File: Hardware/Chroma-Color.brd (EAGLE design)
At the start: 106.4 x 50.5 mm, 92 parts, among them J1 15-91-1102, J2 87832-6422, J3 1775470-6, J4 D2514-6V0C-AR-WD, J7 26-64-4040, U1 EP4CE6E22C8N, U2 ADP3338AKCZ-3.3-RL, U3 ADP3338AKCZ-2.5-RL, U4 NCV565ST12T3G, U5 M25P40-VMN6TPBCT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

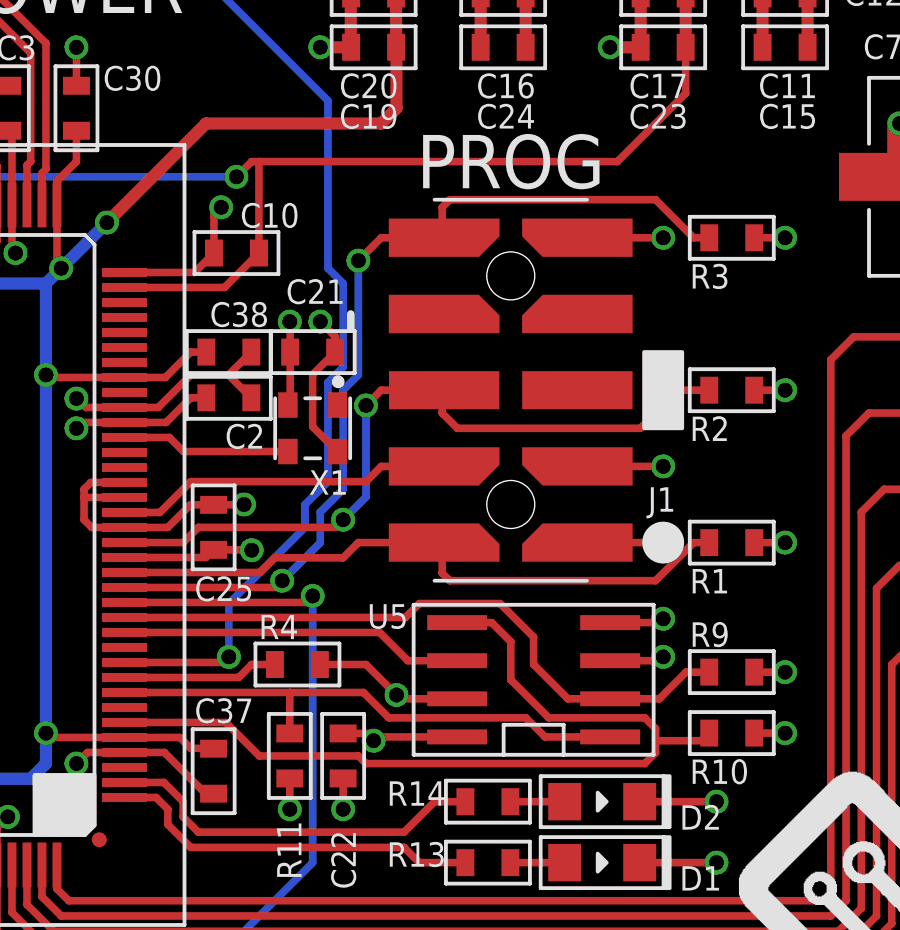
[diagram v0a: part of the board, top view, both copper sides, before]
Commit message: Rev2 start. Fixed JTAG programming cable.
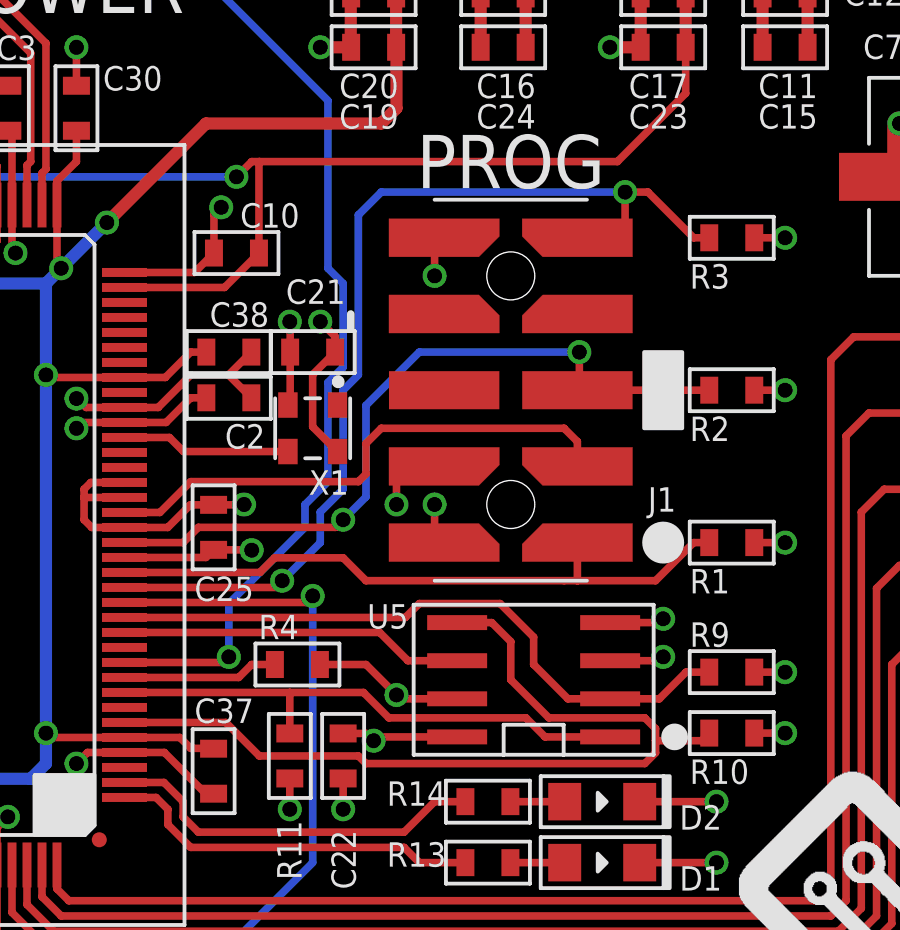
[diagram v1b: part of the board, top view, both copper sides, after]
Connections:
- net 3.3V: now also J1.4; no longer J1.3
- net GND: now also J1.10, J1.2; no longer J1.1, J1.9
- net TCK: now also J1.1; no longer J1.2
- net TDI: now also J1.9; no longer J1.10
- net TDO: now also J1.3; no longer J1.4
- net TMS: now also J1.5; no longer J1.6
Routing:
- net TDO: track 11.3 -> 17.9 mm
- net GND: track 273.3 -> 268.9 mm
- net TDI: track 30.9 -> 34.5 mm

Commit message: Fixed 3 PIN Power Connector.
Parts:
- J7: device PP_Connectors:MOLEX_KK_4_P1 -> PP_Connectors:26-64-4040(KEYPIN1)
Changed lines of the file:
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@@
 <?xml version="1.0" encoding="utf-8"?>
 <!DOCTYPE eagle SYSTEM "eagle.dtd">
-<eagle version="6.5.0">
+<eagle version="6.6.0">
 <drawing>
 <settings>
@@
 <attribute name="NAME" x="89.662" y="8.128" size="1.016" layer="25" font="vector" ratio="16"/>
 </element>
-<element name="J7" library="PP_Connectors" package="MOLEX_KK_4_P1" value="26-64-4040" x="94.996" y="40.386" smashed="yes" rot="R270">
-<attribute name="LABEL02" value="5V" x="100.806" y="37.496" size="1.016" layer="25" font="vector" ratio="16" rot="R90" align="center-left"/>
-<attribute name="LABEL03" value="GND" x="100.702" y="33.178" size="1.016" layer="25" font="vector" ratio="16" rot="R90" align="center-left"/>
-<attribute name="LABEL01" value="12V" x="100.656" y="41.306" size="1.016" layer="25" font="vector" ratio="16" rot="R90" align="center-left"/>
-<attribute name="NAME" x="90.0466" y="31.138" size="1.016" layer="25" font="vector" ratio="16"/>
-</element>
 <element name="C10" library="MF_Passives" package="C0603" value="0.1uF" x="59.944" y="27.178" smashed="yes" rot="R180">
 <attribute name="TOLERANCE" value="N/A" x="59.944" y="27.178" size="1.778" layer="27" rot="R180" display="off"/>
@@
 <element name="FID3" library="MF_Aesthetics" package="FIDUCIAL_0.5MM" value="FIDUCIAL_0.5MM" x="32.766" y="30.226"/>
 <element name="FID4" library="MF_Aesthetics" package="FIDUCIAL_0.5MM" value="FIDUCIAL_0.5MM" x="55.372" y="7.62"/>
+<element name="J7" library="PP_Connectors" package="26-64-4040(KEYPIN1)" value="26-64-4040" x="94.996" y="40.386" smashed="yes" rot="R270">
+<attribute name="LABEL02" value="5V" x="100.806" y="37.75" size="1.016" layer="25" font="vector" ratio="16" rot="R90" align="center-left"/>
+<attribute name="LABEL03" value="GND" x="100.702" y="33.178" size="1.016" layer="25" font="vector" ratio="16" rot="R90" align="center-left"/>
+<attribute name="LABEL01" value="12V" x="100.656" y="41.052" size="1.016" layer="25" font="vector" ratio="16" rot="R90" align="center-left"/>
+<attribute name="NAME" x="101.496" y="48.1294" size="1.016" layer="25" font="vector" ratio="16" rot="R270"/>
+</element>
 </elements>
 <signals>
@@
 <via x="74.168" y="14.986" extent="1-16" drill="0.5"/>
 <wire x1="74.168" y1="14.986" x2="73.152" y2="15.24" width="0.254" layer="2"/>
-<contactref element="J7" pad="4"/>
 <wire x1="8.171" y1="24.071" x2="8.171" y2="22.817" width="0.254" layer="1"/>
 <wire x1="8.171" y1="22.817" x2="8.382" y2="22.606" width="0.254" layer="1"/>
@@
 <wire x1="66.548" y1="17.526" x2="66.548" y2="18.796" width="0.254" layer="1"/>
 <via x="66.548" y="18.796" extent="1-16" drill="0.5"/>
+<contactref element="J7" pad="4"/>
 </signal>
 <signal name="2.5V">
@@
 <contactref element="U3" pad="3"/>
 <contactref element="U4" pad="3"/>
-<contactref element="J7" pad="3"/>
 <wire x1="77.47" y1="41.402" x2="68.58" y2="41.402" width="0.8128" layer="1"/>
 <wire x1="68.58" y1="41.402" x2="68.072" y2="40.894" width="0.8128" layer="1"/>
@@
 <wire x1="86.88" y1="29.972" x2="86.88" y2="29.73" width="0.8128" layer="1"/>
 <wire x1="86.88" y1="29.73" x2="86.868" y2="29.718" width="0.8128" layer="1"/>
-<wire x1="94.996" y1="38.406" x2="97.484" y2="38.406" width="0.8128" layer="1"/>
 <wire x1="97.484" y1="38.406" x2="99.06" y2="36.83" width="0.8128" layer="1"/>
 <wire x1="99.06" y1="36.83" x2="99.06" y2="30.988" width="0.8128" layer="1"/>
@@
 <wire x1="86.301484375" y1="41.402" x2="77.47" y2="41.402" width="0.8128" layer="1"/>
 <contactref element="C9" pad="P$1"/>
-<wire x1="87.134" y1="29.718" x2="87.028" y2="29.718" width="0" layer="19" extent="1-1"/>
+<contactref element="J7" pad="3"/>
+<wire x1="87.028" y1="29.718" x2="87.134" y2="29.718" width="0" layer="19" extent="1-1"/>
+<wire x1="97.484" y1="38.406" x2="94.996" y2="38.406" width="0.8128" layer="1"/>
 </signal>
 <signal name="CLK_50">
@@
 <contactref element="J3" pad="P$5"/>
 <contactref element="J3" pad="P$6"/>
-<contactref element="J7" pad="2"/>
-<wire x1="94.996" y1="42.366" x2="94.996" y2="46.228" width="0.6096" layer="1"/>
 <wire x1="94.996" y1="46.228" x2="91.948" y2="49.276" width="0.6096" layer="1"/>
 <wire x1="91.948" y1="49.276" x2="56.562" y2="49.276" width="0.6096" layer="1"/>
@@
 <wire x1="54.562" y1="48.466" x2="54.562" y2="43.942" width="0.6096" layer="1"/>
 <wire x1="56.562" y1="43.942" x2="56.562" y2="49.276" width="0.6096" layer="1"/>
+<contactref element="J7" pad="2"/>
+<wire x1="94.996" y1="46.228" x2="94.996" y2="42.366" width="0.6096" layer="1"/>
 </signal>
 <signal name="PIN_1">

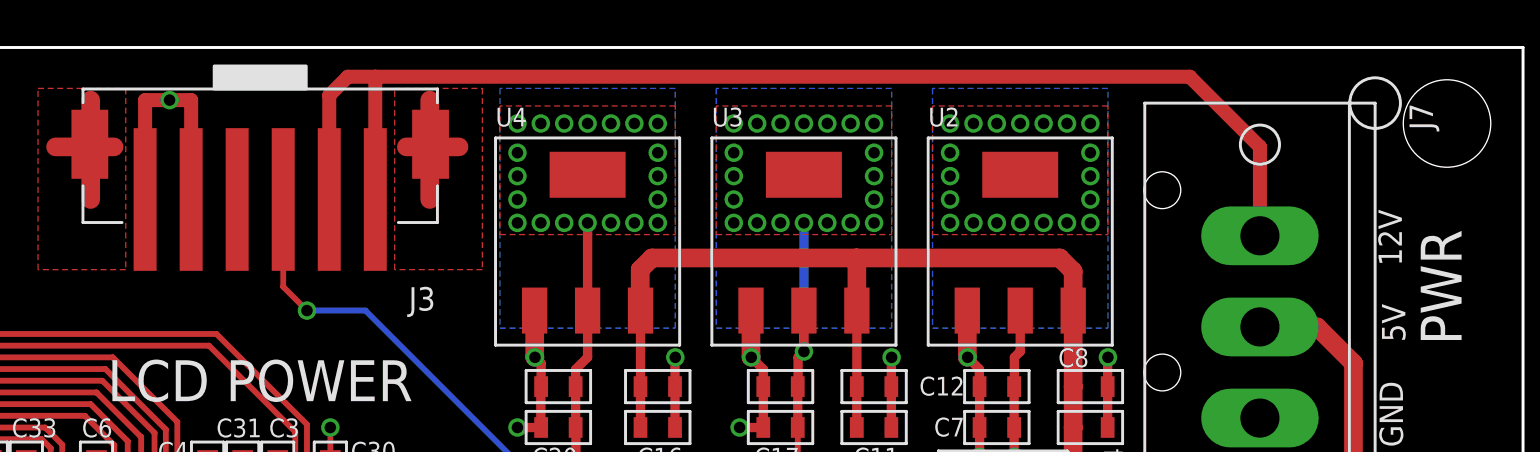
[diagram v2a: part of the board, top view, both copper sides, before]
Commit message: Updated connectors to latest library
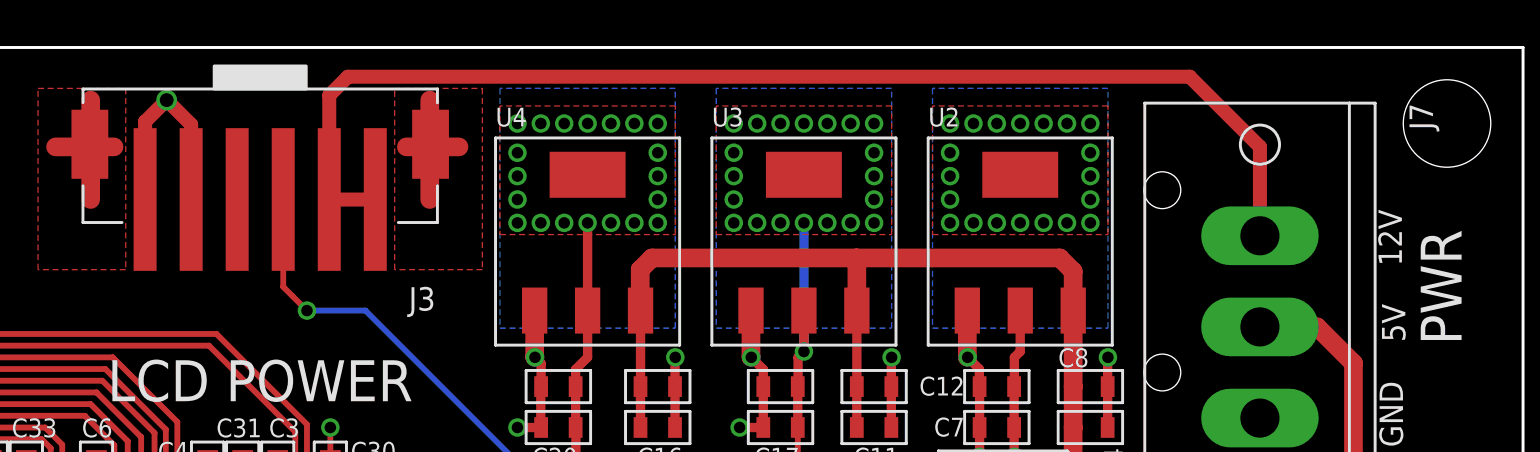
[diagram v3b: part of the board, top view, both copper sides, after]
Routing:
- net 12V: track 55.8 -> 52.4 mm
- net GND: track 268.9 -> 267.8 mm
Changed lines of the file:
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@@
 <attribute name="LABEL28" value="" x="-6.858" y="80.01" size="1.778" layer="27" rot="R180" display="off"/>
 <attribute name="LABEL29" value="" x="-6.858" y="80.01" size="1.778" layer="27" rot="R180" display="off"/>
-<attribute name="LABEL00" value="" x="-6.858" y="80.01" size="1.778" layer="27" rot="R180" display="off"/>
 <attribute name="LABEL01" value="" x="-6.858" y="80.01" size="1.778" layer="27" rot="R180" display="off"/>
 <attribute name="LABEL02" value="" x="-6.858" y="80.01" size="1.778" layer="27" rot="R180" display="off"/>
-</element>
-<element name="J3" library="PP_Connectors" package="1775470-6" value="1775470-6" x="51.562" y="43.942" rot="R180">
-<attribute name="LABEL02" value="" x="5.842" y="104.902" size="1.778" layer="27" rot="R180" display="off"/>
-<attribute name="LABEL03" value="" x="5.842" y="104.902" size="1.778" layer="27" rot="R180" display="off"/>
-<attribute name="LABEL04" value="" x="5.842" y="104.902" size="1.778" layer="27" rot="R180" display="off"/>
-<attribute name="LABEL05" value="" x="5.842" y="104.902" size="1.778" layer="27" rot="R180" display="off"/>
-<attribute name="LABEL00" value="" x="5.842" y="104.902" size="1.778" layer="27" rot="R180" display="off"/>
-<attribute name="LABEL01" value="" x="5.842" y="104.902" size="1.778" layer="27" rot="R180" display="off"/>
+<attribute name="LABEL30" value="" x="22.352" y="44.45" size="1.778" layer="27" rot="R180" display="off"/>
 </element>
 <element name="C22" library="MF_Passives" package="C0603" value="0.1uF" x="63.5" y="10.414" smashed="yes" rot="R270">
@@
 <attribute name="LABEL01" value="12V" x="100.656" y="41.052" size="1.016" layer="25" font="vector" ratio="16" rot="R90" align="center-left"/>
 <attribute name="NAME" x="101.496" y="48.1294" size="1.016" layer="25" font="vector" ratio="16" rot="R270"/>
+</element>
+<element name="J3" library="PP_Connectors" package="1775470-6" value="1775470-6" x="51.562" y="43.942" rot="R180">
+<attribute name="LABEL02" value="" x="51.562" y="43.942" size="1.778" layer="27" rot="R180" display="off"/>
+<attribute name="LABEL03" value="" x="51.562" y="43.942" size="1.778" layer="27" rot="R180" display="off"/>
+<attribute name="LABEL04" value="" x="51.562" y="43.942" size="1.778" layer="27" rot="R180" display="off"/>
+<attribute name="LABEL05" value="" x="51.562" y="43.942" size="1.778" layer="27" rot="R180" display="off"/>
+<attribute name="LABEL06" value="" x="51.562" y="43.942" size="1.778" layer="27" rot="R180" display="off"/>
+<attribute name="LABEL01" value="" x="51.562" y="43.942" size="1.778" layer="27" rot="R180" display="off"/>
 </element>
 </elements>
@@
 <contactref element="J2" pad="P$14"/>
 <contactref element="J2" pad="P$26"/>
-<contactref element="J3" pad="P$2"/>
-<contactref element="J3" pad="P$1"/>
 <contactref element="C22" pad="P$2"/>
 <contactref element="C23" pad="P$2"/>
@@
 <wire x1="32.5135375" y1="16.03" x2="32.258" y2="15.7744625" width="0.254" layer="1"/>
 <wire x1="32.258" y1="15.7744625" x2="32.258" y2="15.53" width="0.254" layer="1"/>
-<wire x1="48.562" y1="43.942" x2="48.562" y2="48.26" width="0.6096" layer="1"/>
-<wire x1="48.562" y1="48.26" x2="47.625" y2="48.26" width="0.6096" layer="1"/>
-<wire x1="47.625" y1="48.26" x2="46.562" y2="48.26" width="0.6096" layer="1"/>
-<wire x1="46.562" y1="48.26" x2="46.562" y2="43.942" width="0.6096" layer="1"/>
-<via x="47.625" y="48.26" extent="1-16" drill="0.5"/>
 <polygon width="0.254" layer="1">
 <vertex x="41.148" y="21.844"/>
@@
 <via x="66.548" y="18.796" extent="1-16" drill="0.5"/>
 <contactref element="J7" pad="4"/>
+<contactref element="J3" pad="P$2"/>
+<contactref element="J3" pad="P$1"/>
+<wire x1="46.562" y1="43.942" x2="46.562" y2="47.324" width="0.6096" layer="1"/>
+<wire x1="46.562" y1="47.324" x2="47.498" y2="48.26" width="0.6096" layer="1"/>
+<wire x1="47.498" y1="48.26" x2="48.562" y2="47.196" width="0.6096" layer="1"/>
+<wire x1="48.562" y1="47.196" x2="48.562" y2="43.942" width="0.6096" layer="1"/>
+<via x="47.498" y="48.26" extent="1-16" drill="0.6"/>
 </signal>
 <signal name="2.5V">
@@
 <contactref element="C9" pad="P$1"/>
 <contactref element="J7" pad="3"/>
-<wire x1="87.028" y1="29.718" x2="87.134" y2="29.718" width="0" layer="19" extent="1-1"/>
 <wire x1="97.484" y1="38.406" x2="94.996" y2="38.406" width="0.8128" layer="1"/>
+<wire x1="87.134" y1="29.718" x2="87.028" y2="29.718" width="0" layer="19" extent="1-1"/>
 </signal>
 <signal name="CLK_50">
@@
 </signal>
 <signal name="PWM/EN">
-<contactref element="J3" pad="P$4"/>
 <contactref element="U1" pad="10"/>
-<wire x1="52.562" y1="43.942" x2="52.562" y2="40.148" width="0.254" layer="1"/>
-<wire x1="52.562" y1="40.148" x2="53.594" y2="39.116" width="0.254" layer="1"/>
 <via x="53.594" y="39.116" extent="1-16" drill="0.5"/>
 <via x="59.69" y="13.716" extent="1-16" drill="0.5"/>
+<wire x1="52.959" y1="39.751" x2="53.594" y2="39.116" width="0.254" layer="1"/>
 <wire x1="59.69" y1="13.716" x2="59.504" y2="13.53" width="0.254" layer="1"/>
 <wire x1="59.504" y1="13.53" x2="56.212" y2="13.53" width="0.254" layer="1"/>
@@
 <wire x1="59.69" y1="13.716" x2="59.69" y2="15.494" width="0.254" layer="16"/>
 <wire x1="59.69" y1="15.494" x2="62.23" y2="18.034" width="0.254" layer="16"/>
+<contactref element="J3" pad="P$4"/>
+<wire x1="52.562" y1="43.942" x2="52.562" y2="40.148" width="0.254" layer="1"/>
+<wire x1="52.562" y1="40.148" x2="52.959" y2="39.751" width="0.254" layer="1"/>
 </signal>
 <signal name="ODD0-">
@@
 </signal>
 <signal name="12V">
+<wire x1="94.996" y1="46.228" x2="91.948" y2="49.276" width="0.6096" layer="1"/>
+<wire x1="91.948" y1="49.276" x2="55.372" y2="49.276" width="0.6096" layer="1"/>
+<wire x1="55.372" y1="49.276" x2="54.562" y2="48.466" width="0.6096" layer="1"/>
+<contactref element="J7" pad="2"/>
+<wire x1="94.996" y1="46.228" x2="94.996" y2="42.366" width="0.6096" layer="1"/>
 <contactref element="J3" pad="P$5"/>
 <contactref element="J3" pad="P$6"/>
-<wire x1="94.996" y1="46.228" x2="91.948" y2="49.276" width="0.6096" layer="1"/>
-<wire x1="91.948" y1="49.276" x2="56.562" y2="49.276" width="0.6096" layer="1"/>
-<wire x1="56.562" y1="49.276" x2="55.372" y2="49.276" width="0.6096" layer="1"/>
-<wire x1="55.372" y1="49.276" x2="54.562" y2="48.466" width="0.6096" layer="1"/>
 <wire x1="54.562" y1="48.466" x2="54.562" y2="43.942" width="0.6096" layer="1"/>
-<wire x1="56.562" y1="43.942" x2="56.562" y2="49.276" width="0.6096" layer="1"/>
-<contactref element="J7" pad="2"/>
-<wire x1="94.996" y1="46.228" x2="94.996" y2="42.366" width="0.6096" layer="1"/>
+<wire x1="54.562" y1="43.942" x2="56.562" y2="43.942" width="0.6096" layer="1"/>
 </signal>
 <signal name="PIN_1">

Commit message: Fixed voltage regulators to use newer library
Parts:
- U2, U3: device PP_PowerIC:SOT-223B -> PP_PowerIC:ADP3338_SOT-223-3
- U4: device PP_PowerIC:SOT-223B -> PP_PowerIC:NCV565_SOT-223-3
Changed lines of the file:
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@@
 <attribute name="NAME" x="63.37" y="32.342" size="0.8128" layer="25" font="vector" ratio="16"/>
 </element>
-<element name="U2" library="PP_PowerIC" package="SOT-223B" value="ADP3338AKCZ-3.3-RL" x="84.582" y="41.656"/>
-<element name="U3" library="PP_PowerIC" package="SOT-223B" value="ADP3338AKCZ-2.5-RL" x="75.184" y="41.656"/>
-<element name="U4" library="PP_PowerIC" package="SOT-223B" value="NCV565ST12T3G" x="65.786" y="41.656"/>
+<element name="U2" library="PP_PowerIC" package="ADP3338_SOT-223-3" value="ADP3338AKCZ-3.3-RL" x="84.582" y="41.656"/>
+<element name="U3" library="PP_PowerIC" package="ADP3338_SOT-223-3" value="ADP3338AKCZ-2.5-RL" x="75.184" y="41.656"/>
+<element name="U4" library="PP_PowerIC" package="NCV565_SOT-223-3" value="NCV565ST12T3G" x="65.786" y="41.656"/>
 <element name="U5" library="PP_DigitalIC" package="SOIC-8" value="M25P40-VMN6TPBCT" x="69.85" y="12.954" smashed="yes" rot="R90">
 <attribute name="NAME" x="64.302" y="14.66" size="0.8128" layer="21" font="vector" ratio="16"/>
